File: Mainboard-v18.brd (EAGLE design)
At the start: 50 x 50 mm, 35 parts, among them T1 2N3904, T2 2N3904

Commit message: modified:   Mainboard-v18.brd 	modified:   Mainboard-v18.pdf 	modified:   Mainboard-v18.sch 	new file:   Mainboard-v18_top.pdf
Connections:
- new net N$3: U$34.1
- net GND: no longer U$34.1
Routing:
- net GND: track 50.1 -> 27.0 mm
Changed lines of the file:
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@@
 <layer number="17" name="Pads" color="2" fill="1" visible="yes" active="yes"/>
 <layer number="18" name="Vias" color="2" fill="1" visible="yes" active="yes"/>
-<layer number="19" name="Unrouted" color="6" fill="1" visible="no" active="yes"/>
-<layer number="20" name="Dimension" color="6" fill="1" visible="no" active="yes"/>
-<layer number="21" name="tPlace" color="15" fill="1" visible="no" active="yes"/>
-<layer number="22" name="bPlace" color="7" fill="1" visible="no" active="yes"/>
-<layer number="23" name="tOrigins" color="15" fill="1" visible="no" active="yes"/>
-<layer number="24" name="bOrigins" color="15" fill="1" visible="no" active="yes"/>
-<layer number="25" name="tNames" color="7" fill="1" visible="no" active="yes"/>
-<layer number="26" name="bNames" color="7" fill="1" visible="no" active="yes"/>
-<layer number="27" name="tValues" color="7" fill="1" visible="no" active="yes"/>
-<layer number="28" name="bValues" color="7" fill="1" visible="no" active="yes"/>
-<layer number="29" name="tStop" color="5" fill="1" visible="no" active="yes"/>
-<layer number="30" name="bStop" color="7" fill="6" visible="no" active="yes"/>
-<layer number="31" name="tCream" color="7" fill="4" visible="no" active="yes"/>
-<layer number="32" name="bCream" color="7" fill="5" visible="no" active="yes"/>
-<layer number="33" name="tFinish" color="6" fill="3" visible="no" active="yes"/>
-<layer number="34" name="bFinish" color="6" fill="6" visible="no" active="yes"/>
-<layer number="35" name="tGlue" color="7" fill="4" visible="no" active="yes"/>
-<layer number="36" name="bGlue" color="7" fill="5" visible="no" active="yes"/>
-<layer number="37" name="tTest" color="7" fill="1" visible="no" active="yes"/>
-<layer number="38" name="bTest" color="7" fill="1" visible="no" active="yes"/>
-<layer number="39" name="tKeepout" color="4" fill="11" visible="no" active="yes"/>
-<layer number="40" name="bKeepout" color="1" fill="11" visible="no" active="yes"/>
-<layer number="41" name="tRestrict" color="4" fill="10" visible="no" active="yes"/>
-<layer number="42" name="bRestrict" color="1" fill="10" visible="no" active="yes"/>
-<layer number="43" name="vRestrict" color="2" fill="10" visible="no" active="yes"/>
-<layer number="44" name="Drills" color="7" fill="1" visible="no" active="yes"/>
-<layer number="45" name="Holes" color="7" fill="1" visible="no" active="yes"/>
-<layer number="46" name="Milling" color="3" fill="1" visible="no" active="yes"/>
-<layer number="47" name="Measures" color="7" fill="1" visible="no" active="yes"/>
-<layer number="48" name="Document" color="7" fill="1" visible="no" active="yes"/>
-<layer number="49" name="Reference" color="7" fill="1" visible="no" active="yes"/>
-<layer number="50" name="dxf" color="7" fill="1" visible="no" active="yes"/>
-<layer number="51" name="tDocu" color="14" fill="1" visible="no" active="yes"/>
-<layer number="52" name="bDocu" color="7" fill="1" visible="no" active="yes"/>
+<layer number="19" name="Unrouted" color="6" fill="1" visible="yes" active="yes"/>
+<layer number="20" name="Dimension" color="6" fill="1" visible="yes" active="yes"/>
+<layer number="21" name="tPlace" color="15" fill="1" visible="yes" active="yes"/>
+<layer number="22" name="bPlace" color="7" fill="1" visible="yes" active="yes"/>
+<layer number="23" name="tOrigins" color="15" fill="1" visible="yes" active="yes"/>
+<layer number="24" name="bOrigins" color="15" fill="1" visible="yes" active="yes"/>
+<layer number="25" name="tNames" color="7" fill="1" visible="yes" active="yes"/>
+<layer number="26" name="bNames" color="7" fill="1" visible="yes" active="yes"/>
+<layer number="27" name="tValues" color="7" fill="1" visible="yes" active="yes"/>
+<layer number="28" name="bValues" color="7" fill="1" visible="yes" active="yes"/>
+<layer number="29" name="tStop" color="5" fill="1" visible="yes" active="yes"/>
+<layer number="30" name="bStop" color="7" fill="6" visible="yes" active="yes"/>
+<layer number="31" name="tCream" color="7" fill="4" visible="yes" active="yes"/>
+<layer number="32" name="bCream" color="7" fill="5" visible="yes" active="yes"/>
+<layer number="33" name="tFinish" color="6" fill="3" visible="yes" active="yes"/>
+<layer number="34" name="bFinish" color="6" fill="6" visible="yes" active="yes"/>
+<layer number="35" name="tGlue" color="7" fill="4" visible="yes" active="yes"/>
+<layer number="36" name="bGlue" color="7" fill="5" visible="yes" active="yes"/>
+<layer number="37" name="tTest" color="7" fill="1" visible="yes" active="yes"/>
+<layer number="38" name="bTest" color="7" fill="1" visible="yes" active="yes"/>
+<layer number="39" name="tKeepout" color="4" fill="11" visible="yes" active="yes"/>
+<layer number="40" name="bKeepout" color="1" fill="11" visible="yes" active="yes"/>
+<layer number="41" name="tRestrict" color="4" fill="10" visible="yes" active="yes"/>
+<layer number="42" name="bRestrict" color="1" fill="10" visible="yes" active="yes"/>
+<layer number="43" name="vRestrict" color="2" fill="10" visible="yes" active="yes"/>
+<layer number="44" name="Drills" color="7" fill="1" visible="yes" active="yes"/>
+<layer number="45" name="Holes" color="7" fill="1" visible="yes" active="yes"/>
+<layer number="46" name="Milling" color="3" fill="1" visible="yes" active="yes"/>
+<layer number="47" name="Measures" color="7" fill="1" visible="yes" active="yes"/>
+<layer number="48" name="Document" color="7" fill="1" visible="yes" active="yes"/>
+<layer number="49" name="Reference" color="7" fill="1" visible="yes" active="yes"/>
+<layer number="50" name="dxf" color="7" fill="1" visible="yes" active="yes"/>
+<layer number="51" name="tDocu" color="14" fill="1" visible="yes" active="yes"/>
+<layer number="52" name="bDocu" color="7" fill="1" visible="yes" active="yes"/>
 <layer number="53" name="tGND_GNDA" color="7" fill="9" visible="no" active="no"/>
 <layer number="54" name="bGND_GNDA" color="1" fill="9" visible="no" active="no"/>
-<layer number="56" name="wert" color="7" fill="1" visible="no" active="yes"/>
+<layer number="56" name="wert" color="7" fill="1" visible="yes" active="yes"/>
 <layer number="91" name="Nets" color="2" fill="1" visible="no" active="no"/>
 <layer number="92" name="Busses" color="1" fill="1" visible="no" active="no"/>
@@
 <layer number="98" name="Guide" color="6" fill="1" visible="no" active="no"/>
 <layer number="100" name="Muster" color="7" fill="1" visible="no" active="no"/>
-<layer number="101" name="Patch_Top" color="12" fill="4" visible="no" active="yes"/>
-<layer number="102" name="Vscore" color="7" fill="1" visible="no" active="yes"/>
-<layer number="104" name="Name" color="7" fill="1" visible="no" active="yes"/>
-<layer number="116" name="Patch_BOT" color="9" fill="4" visible="no" active="yes"/>
-<layer number="121" name="_tsilk" color="7" fill="1" visible="no" active="yes"/>
-<layer number="122" name="_bsilk" color="7" fill="1" visible="no" active="yes"/>
-<layer number="151" name="HeatSink" color="7" fill="1" visible="no" active="yes"/>
+<layer number="101" name="Patch_Top" color="12" fill="4" visible="yes" active="yes"/>
+<layer number="102" name="Vscore" color="7" fill="1" visible="yes" active="yes"/>
+<layer number="104" name="Name" color="7" fill="1" visible="yes" active="yes"/>
+<layer number="116" name="Patch_BOT" color="9" fill="4" visible="yes" active="yes"/>
+<layer number="121" name="_tsilk" color="7" fill="1" visible="yes" active="yes"/>
+<layer number="122" name="_bsilk" color="7" fill="1" visible="yes" active="yes"/>
+<layer number="151" name="HeatSink" color="7" fill="1" visible="yes" active="yes"/>
 <layer number="200" name="200bmp" color="1" fill="10" visible="no" active="no"/>
 <layer number="201" name="201bmp" color="2" fill="1" visible="no" active="no"/>
@@
 <layer number="250" name="Descript" color="3" fill="1" visible="no" active="no"/>
 <layer number="251" name="SMDround" color="12" fill="11" visible="no" active="no"/>
-<layer number="254" name="cooling" color="7" fill="1" visible="no" active="yes"/>
+<layer number="254" name="cooling" color="7" fill="1" visible="yes" active="yes"/>
 </layers>
 <board>
@@
 <contactref element="U$30" pad="1"/>
 <contactref element="PAD3" pad="1"/>
-<contactref element="U$34" pad="1"/>
 <contactref element="T1" pad="3"/>
 <contactref element="T2" pad="3"/>
@@
 </polygon>
 <wire x1="46.4127" y1="35.69755625" x2="48.12030625" y2="29.75571875" width="0.4064" layer="16"/>
-<wire x1="48.12030625" y1="29.75571875" x2="29.5" y2="27" width="0.4064" layer="16"/>
-<wire x1="29.5" y1="27" x2="34" y2="24.5" width="0.4064" layer="16"/>
-<wire x1="34" y1="24.5" x2="33.02" y2="21.59" width="0.4064" layer="16"/>
-<wire x1="32.771578125" y1="47.471203125" x2="30.5" y2="40.5" width="0.4064" layer="16"/>
-<wire x1="30.5" y1="40.5" x2="24.5" y2="40" width="0.4064" layer="16"/>
-<wire x1="24.5" y1="40" x2="24.5" y2="36.5" width="0.4064" layer="16"/>
 <contactref element="PAD8" pad="1"/>
+<wire x1="48.12030625" y1="29.75571875" x2="33" y2="27" width="0.4064" layer="16"/>
+<wire x1="33" y1="27" x2="33.02" y2="21.59" width="0.4064" layer="16"/>
+</signal>
+<signal name="N$3">
+<contactref element="U$34" pad="1"/>
 </signal>
 </signals>

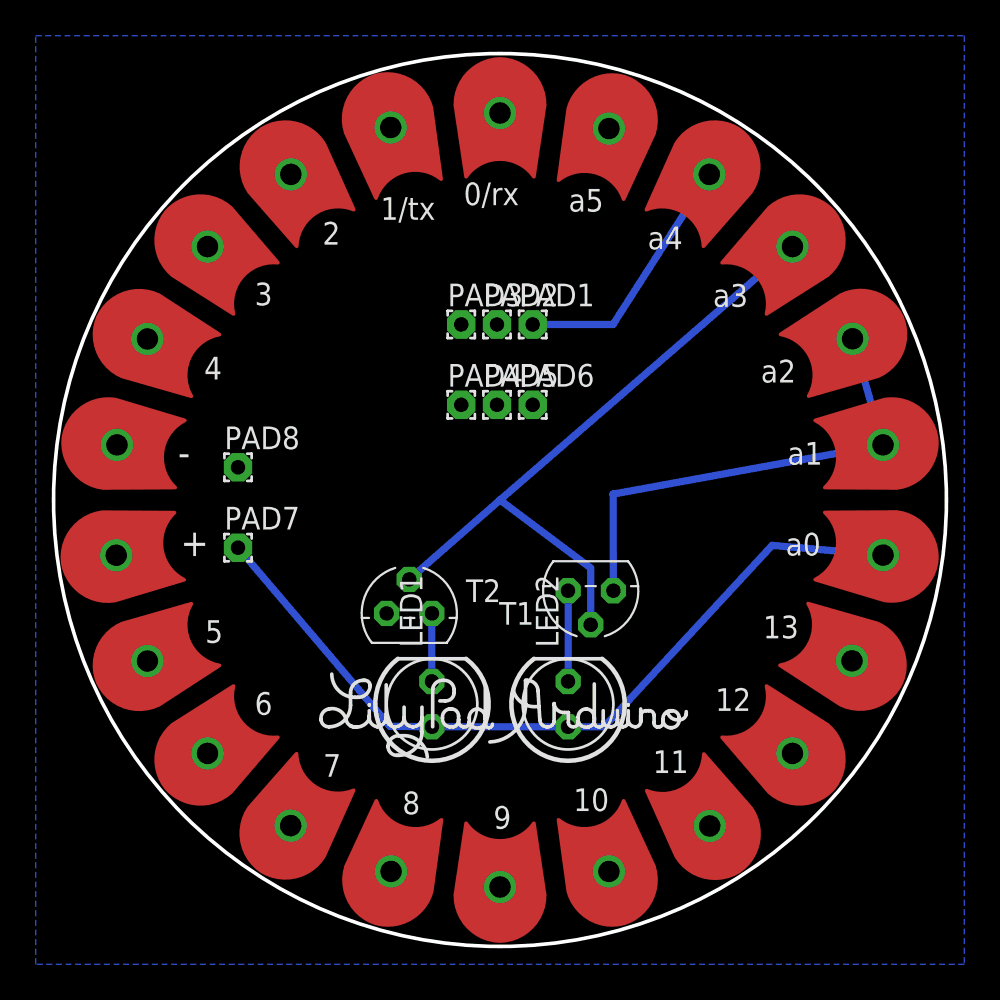
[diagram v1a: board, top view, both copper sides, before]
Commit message: modified:   Mainboard-v18.brd 	modified:   Mainboard-v18.sch
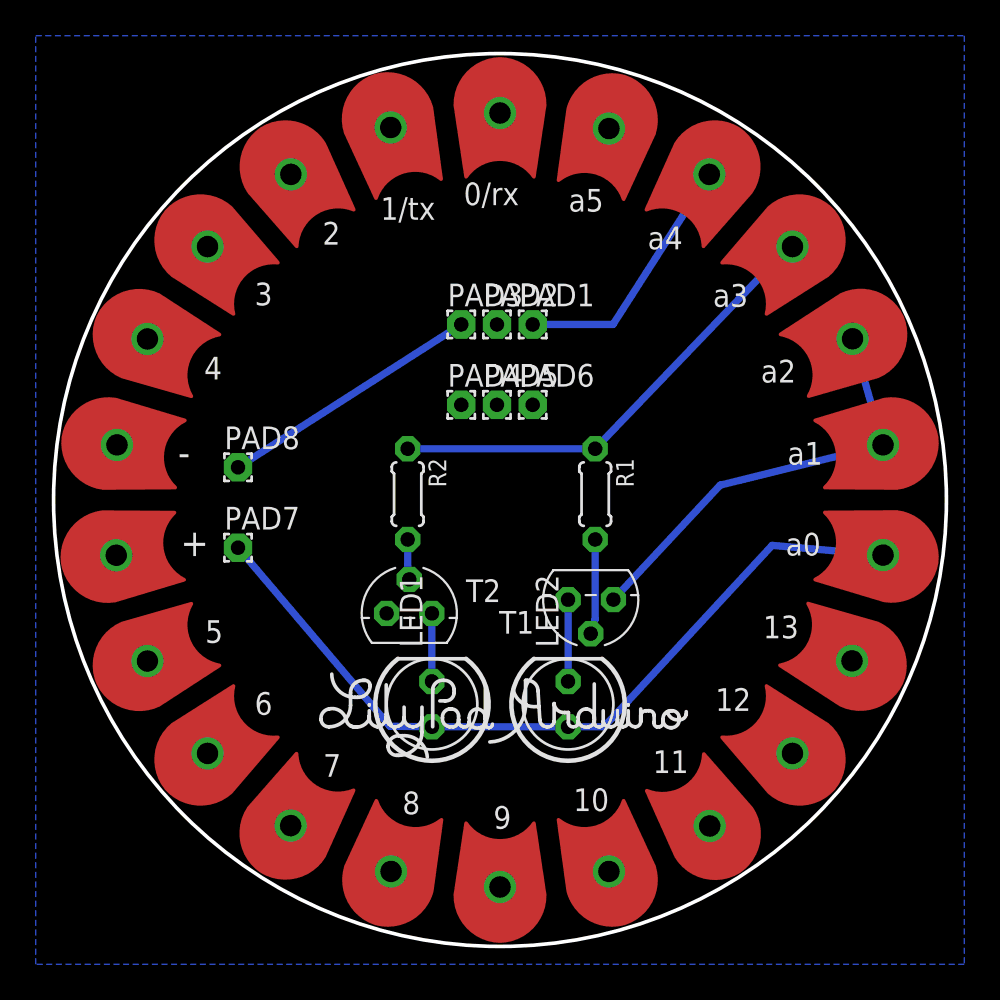
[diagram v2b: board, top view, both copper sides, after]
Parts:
- added R1, R2: (no value), resistor:0204/5
- moved T1 0.50 mm to (31.8, 21.1)
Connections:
- new net N$4: R2.2, T2.2
- new net N$5: R1.2, T1.2
- net A3: now also R1.1, R2.1; no longer T1.2, T2.2
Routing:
- net GND: track 27.0 -> 39.2 mm
- net A3: track 37.9 -> 26.5 mm
- net N$5: track 0.00 -> 5.31 mm
- net N$4: track 0.00 -> 2.24 mm
- net N$2: track 5.08 -> 4.58 mm
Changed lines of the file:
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@@
 <element name="U$4" library="LilyPad-Wearables" package="SEWTAP" value="SEWTAP1" x="48.15" y="23.58" rot="R171.8"/>
 <element name="U$1" library="LilyPad-Wearables" package="LOGO-LPA" value="LOGO-LPLPA" x="26.67" y="14.97"/>
-<element name="T1" library="transistor" package="TO92" value="2N3904" x="31.75" y="21.59" rot="R180"/>
+<element name="T1" library="transistor" package="TO92" value="2N3904" x="31.75" y="21.09" rot="R180"/>
 <element name="T2" library="transistor" package="TO92" value="2N3904" x="21.59" y="20.32"/>
 <element name="LED1" library="led" package="LED5MM" value="" x="22.86" y="15.24" rot="R90"/>
@@
 <element name="PAD7" library="wirepad" package="1,6/0,8" value="" x="12" y="24"/>
 <element name="PAD8" library="wirepad" package="1,6/0,8" value="" x="12" y="28.5"/>
+<element name="R1" library="resistor" package="0204/5" value="" x="32" y="27" rot="R270"/>
+<element name="R2" library="resistor" package="0204/5" value="" x="21.5" y="27" rot="R270"/>
 </elements>
 <signals>
@@
 <signal name="A3">
 <contactref element="U$32" pad="1"/>
-<contactref element="T1" pad="2"/>
-<contactref element="T2" pad="2"/>
-<wire x1="43.047321875" y1="40.86035625" x2="26.67" y2="26.67" width="0.4064" layer="16"/>
-<wire x1="26.67" y1="26.67" x2="31.75" y2="22.86" width="0.4064" layer="16"/>
-<wire x1="31.75" y1="22.86" x2="31.75" y2="19.685" width="0.4064" layer="16"/>
-<wire x1="26.67" y1="26.67" x2="21.59" y2="22.225" width="0.4064" layer="16"/>
+<contactref element="R2" pad="1"/>
+<contactref element="R1" pad="1"/>
+<wire x1="43.047321875" y1="40.86035625" x2="43" y2="41" width="0.4064" layer="16"/>
+<wire x1="43" y1="41" x2="32" y2="29.54" width="0.4064" layer="16"/>
+<wire x1="32" y1="29.54" x2="21.5" y2="29.54" width="0.4064" layer="16"/>
 </signal>
 <signal name="A4">
@@
 <contactref element="T1" pad="1"/>
 <contactref element="LED2" pad="K"/>
-<wire x1="30.48" y1="21.59" x2="30.48" y2="16.51" width="0.4064" layer="16"/>
+<wire x1="30.48" y1="16.51" x2="30.48" y2="21.09" width="0.4064" layer="16"/>
 </signal>
 <signal name="GND">
@@
 <wire x1="46.4127" y1="35.69755625" x2="48.12030625" y2="29.75571875" width="0.4064" layer="16"/>
 <contactref element="PAD8" pad="1"/>
-<wire x1="48.12030625" y1="29.75571875" x2="33" y2="27" width="0.4064" layer="16"/>
-<wire x1="33" y1="27" x2="33.02" y2="21.59" width="0.4064" layer="16"/>
+<wire x1="24.5" y1="36.5" x2="12" y2="28.5" width="0.4064" layer="16"/>
+<wire x1="48.12030625" y1="29.75571875" x2="39" y2="27.5" width="0.4064" layer="16"/>
+<wire x1="39" y1="27.5" x2="33.02" y2="21.09" width="0.4064" layer="16"/>
 </signal>
 <signal name="N$3">
 <contactref element="U$34" pad="1"/>
 </signal>
+<signal name="N$4">
+<contactref element="T2" pad="2"/>
+<contactref element="R2" pad="2"/>
+<wire x1="21.5" y1="24.46" x2="21.5" y2="23" width="0.4064" layer="16"/>
+<wire x1="21.5" y1="23" x2="21.59" y2="22.225" width="0.4064" layer="16"/>
+</signal>
+<signal name="N$5">
+<contactref element="T1" pad="2"/>
+<contactref element="R1" pad="2"/>
+<wire x1="32" y1="24.46" x2="32" y2="20" width="0.4064" layer="16"/>
+<wire x1="32" y1="20" x2="31.75" y2="19.185" width="0.4064" layer="16"/>
+</signal>
 </signals>

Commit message: finish
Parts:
- moved R1 0.25 mm to (31.8, 27.0)
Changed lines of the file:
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@@
 <setting verticaltext="up"/>
 </settings>
-<grid distance="0.5" unitdist="mm" unit="mm" style="dots" multiple="1" display="yes" altdistance="0.1" altunitdist="mm" altunit="mm"/>
+<grid distance="0.25" unitdist="mm" unit="mm" style="dots" multiple="1" display="yes" altdistance="0.1" altunitdist="mm" altunit="mm"/>
 <layers>
 <layer number="1" name="Top" color="4" fill="1" visible="yes" active="yes"/>
@@
 <element name="PAD7" library="wirepad" package="1,6/0,8" value="" x="12" y="24"/>
 <element name="PAD8" library="wirepad" package="1,6/0,8" value="" x="12" y="28.5"/>
-<element name="R1" library="resistor" package="0204/5" value="" x="32" y="27" rot="R270"/>
+<element name="R1" library="resistor" package="0204/5" value="" x="31.75" y="27" rot="R270"/>
 <element name="R2" library="resistor" package="0204/5" value="" x="21.5" y="27" rot="R270"/>
 </elements>
@@
 <contactref element="R2" pad="1"/>
 <contactref element="R1" pad="1"/>
-<wire x1="43.047321875" y1="40.86035625" x2="43" y2="41" width="0.4064" layer="16"/>
-<wire x1="43" y1="41" x2="32" y2="29.54" width="0.4064" layer="16"/>
-<wire x1="32" y1="29.54" x2="21.5" y2="29.54" width="0.4064" layer="16"/>
+<wire x1="21.5" y1="29.54" x2="31.75" y2="29.54" width="0.4064" layer="16"/>
+<wire x1="43.047321875" y1="40.86035625" x2="31.75" y2="29.54" width="0.4064" layer="16"/>
 </signal>
 <signal name="A4">
@@
 <contactref element="T2" pad="2"/>
 <contactref element="R2" pad="2"/>
-<wire x1="21.5" y1="24.46" x2="21.5" y2="23" width="0.4064" layer="16"/>
-<wire x1="21.5" y1="23" x2="21.59" y2="22.225" width="0.4064" layer="16"/>
+<wire x1="21.5" y1="24.46" x2="21.5" y2="22.75" width="0.4064" layer="16"/>
+<wire x1="21.5" y1="22.75" x2="21.59" y2="22.225" width="0.4064" layer="16"/>
 </signal>
 <signal name="N$5">
 <contactref element="T1" pad="2"/>
 <contactref element="R1" pad="2"/>
-<wire x1="32" y1="24.46" x2="32" y2="20" width="0.4064" layer="16"/>
-<wire x1="32" y1="20" x2="31.75" y2="19.185" width="0.4064" layer="16"/>
+<wire x1="31.75" y1="24.46" x2="31.75" y2="19.185" width="0.4064" layer="16"/>
 </signal>
 </signals>
